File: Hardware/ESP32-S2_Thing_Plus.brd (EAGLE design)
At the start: 22.9 x 64.8 mm, 147 parts, among them J3 QWIIC_RA, J5 USB-C, J6 JTAG, Q1 2.5A/30V, Q2 MBT3904DW1T1, U1 ESP32-S2-WROOM, U2 CP210X, U3 AP2112, U4 MCP73831, U5 TC7USB40MU, Y1 32.768kHz

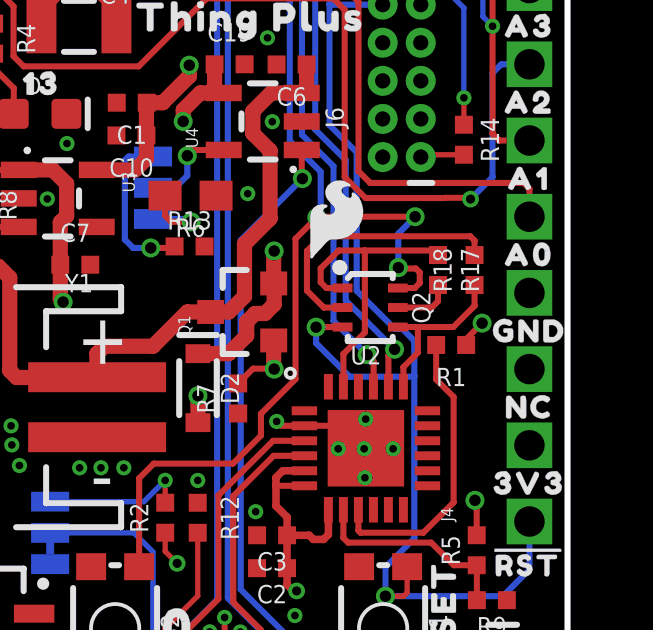
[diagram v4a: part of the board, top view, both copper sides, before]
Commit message: eng run checklist
-one proportional font in sch fixed.
-updated auto-reset paragraph in sch to reflect S2 strapping pins
-updated USB selection jumper paragraph to more clearly show options and default.
-removed S2 Module dimensions from footprint (forgot about them while doing the library work early on)
-added more dimensions for header rows
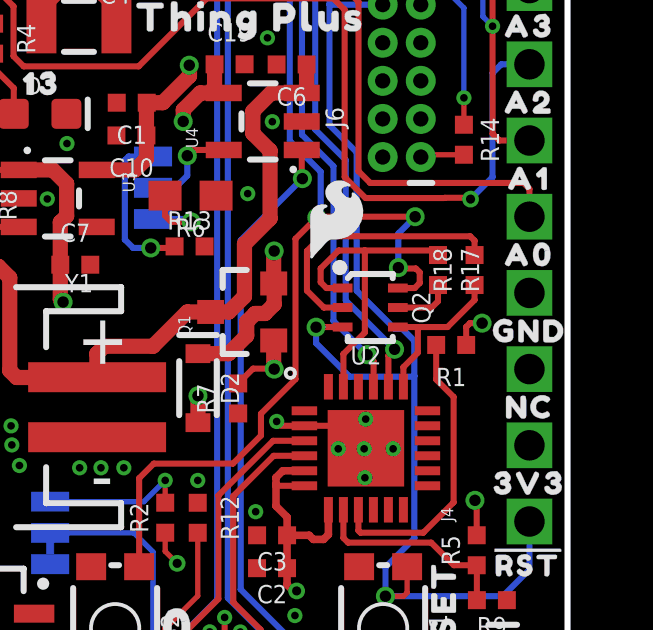
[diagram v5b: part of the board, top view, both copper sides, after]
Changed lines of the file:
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@@
 <layers>
 <layer number="1" name="Top" color="4" fill="1" visible="yes" active="yes"/>
-<layer number="2" name="Route2" color="1" fill="3" visible="no" active="yes"/>
-<layer number="15" name="Route15" color="4" fill="6" visible="no" active="yes"/>
+<layer number="2" name="Route2" color="1" fill="3" visible="yes" active="yes"/>
+<layer number="15" name="Route15" color="4" fill="6" visible="yes" active="yes"/>
 <layer number="16" name="Bottom" color="1" fill="1" visible="yes" active="yes"/>
 <layer number="17" name="Pads" color="2" fill="1" visible="yes" active="yes"/>
 <layer number="18" name="Vias" color="2" fill="1" visible="yes" active="yes"/>
 <layer number="19" name="Unrouted" color="6" fill="1" visible="yes" active="yes"/>
-<layer number="20" name="Dimension" color="24" fill="1" visible="no" active="yes"/>
-<layer number="21" name="tPlace" color="16" fill="1" visible="no" active="yes"/>
-<layer number="22" name="bPlace" color="14" fill="1" visible="no" active="yes"/>
-<layer number="23" name="tOrigins" color="15" fill="1" visible="no" active="yes"/>
-<layer number="24" name="bOrigins" color="15" fill="1" visible="no" active="yes"/>
+<layer number="20" name="Dimension" color="24" fill="1" visible="yes" active="yes"/>
+<layer number="21" name="tPlace" color="16" fill="1" visible="yes" active="yes"/>
+<layer number="22" name="bPlace" color="14" fill="1" visible="yes" active="yes"/>
+<layer number="23" name="tOrigins" color="15" fill="1" visible="yes" active="yes"/>
+<layer number="24" name="bOrigins" color="15" fill="1" visible="yes" active="yes"/>
 <layer number="25" name="tNames" color="7" fill="1" visible="no" active="yes"/>
 <layer number="26" name="bNames" color="7" fill="1" visible="no" active="yes"/>
@@
 <layer number="43" name="vRestrict" color="2" fill="10" visible="no" active="yes"/>
 <layer number="44" name="Drills" color="7" fill="1" visible="no" active="yes"/>
-<layer number="45" name="Holes" color="7" fill="1" visible="no" active="yes"/>
+<layer number="45" name="Holes" color="7" fill="1" visible="yes" active="yes"/>
 <layer number="46" name="Milling" color="3" fill="1" visible="no" active="yes"/>
 <layer number="47" name="Measures" color="7" fill="1" visible="no" active="yes"/>
 <layer number="48" name="Document" color="7" fill="1" visible="no" active="yes"/>
-<layer number="49" name="Reference" color="7" fill="1" visible="no" active="yes"/>
-<layer number="51" name="tDocu" color="6" fill="1" visible="no" active="yes"/>
+<layer number="49" name="Reference" color="7" fill="1" visible="yes" active="yes"/>
+<layer number="51" name="tDocu" color="6" fill="1" visible="yes" active="yes"/>
 <layer number="52" name="bDocu" color="7" fill="1" visible="no" active="yes"/>
 <layer number="3" name="Route3" color="4" fill="3" visible="no" active="no"/>
@@
 <rectangle x1="16.09216875" y1="14.893290625" x2="16.15820625" y2="15.154909375" layer="41" rot="R90"/>
 <rectangle x1="16.07946875" y1="17.67713125" x2="16.14550625" y2="17.93875" layer="41" rot="R90"/>
+<dimension x1="2.54" y1="0" x2="1.27" y2="24.13" x3="-21.59" y3="12.065" textsize="1.778" layer="47" dtype="vertical" unit="inch" visible="yes"/>
+<dimension x1="20.32" y1="0" x2="21.59" y2="13.97" x3="33.02" y3="6.985" textsize="1.778" layer="47" dtype="vertical" unit="inch" visible="yes"/>
+<dimension x1="2.54" y1="0" x2="1.27" y2="52.07" x3="-25.4" y3="26.035" textsize="1.778" layer="47" dtype="vertical" unit="inch" visible="yes"/>
+<dimension x1="20.32" y1="0" x2="21.59" y2="52.07" x3="36.83" y3="26.035" textsize="1.778" layer="47" dtype="vertical" unit="inch" visible="yes"/>
 </plain>
 <attributes>
@@
 <wire x1="13.136878125" y1="15.19935625" x2="13.1419625" y2="15.204440625" width="0.2032" layer="1"/>
 <wire x1="13.1419625" y1="15.204440625" x2="13.14958125" y2="15.212059375" width="0.2032" layer="1"/>
-<wire x1="19.481421875" y1="19.85518125" x2="19.481421875" y2="20.05038125" width="0.2032" layer="1"/>
-<wire x1="20.0126625" y1="20.581621875" x2="19.481421875" y2="20.05038125" width="0.2032" layer="1"/>
+<wire x1="19.481421875" y1="19.85518125" x2="19.481421875" y2="20.45678125" width="0.2032" layer="1"/>
+<wire x1="20.0126625" y1="20.581621875" x2="19.6062625" y2="20.581621875" width="0.2032" layer="1"/>
+<wire x1="19.6062625" y1="20.581621875" x2="19.481421875" y2="20.45678125" width="0.2032" layer="1"/>
 <via x="20.0126625" y="20.581621875" extent="1-16" drill="0.381"/>
 <via x="9.847578125" y="12.5755375" extent="1-16" drill="0.3048"/>
@@
 <contactref element="U2" pad="19"/>
 <wire x1="17.871440625" y1="20.452321875" x2="17.203940625" y2="20.452321875" width="0.2032" layer="1"/>
-<wire x1="19.7612" y1="21.852" x2="19.7612" y2="21.1582" width="0.2032" layer="1"/>
-<wire x1="19.055321875" y1="20.452321875" x2="17.871440625" y2="20.452321875" width="0.2032" layer="1"/>
-<wire x1="19.7612" y1="21.1582" x2="19.055321875" y2="20.452321875" width="0.2032" layer="1"/>
+<wire x1="19.7612" y1="21.852" x2="19.7612" y2="21.353778125" width="0.2032" layer="1"/>
+<wire x1="18.85974375" y1="20.452321875" x2="17.871440625" y2="20.452321875" width="0.2032" layer="1"/>
+<wire x1="19.7612" y1="21.353778125" x2="18.85974375" y2="20.452321875" width="0.2032" layer="1"/>
 <wire x1="17.3891625" y1="18.460940625" x2="17.3891625" y2="19.1163625" width="0.2032" layer="1"/>
 <wire x1="17.871440625" y1="19.598640625" x2="17.871440625" y2="20.452321875" width="0.2032" layer="1"/>
